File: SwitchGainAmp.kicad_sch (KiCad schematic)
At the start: 22 parts, among them Q3 BSS138, Q4 BSS138, Q5 BSS138, Q6 BSS138, U8 LT1493

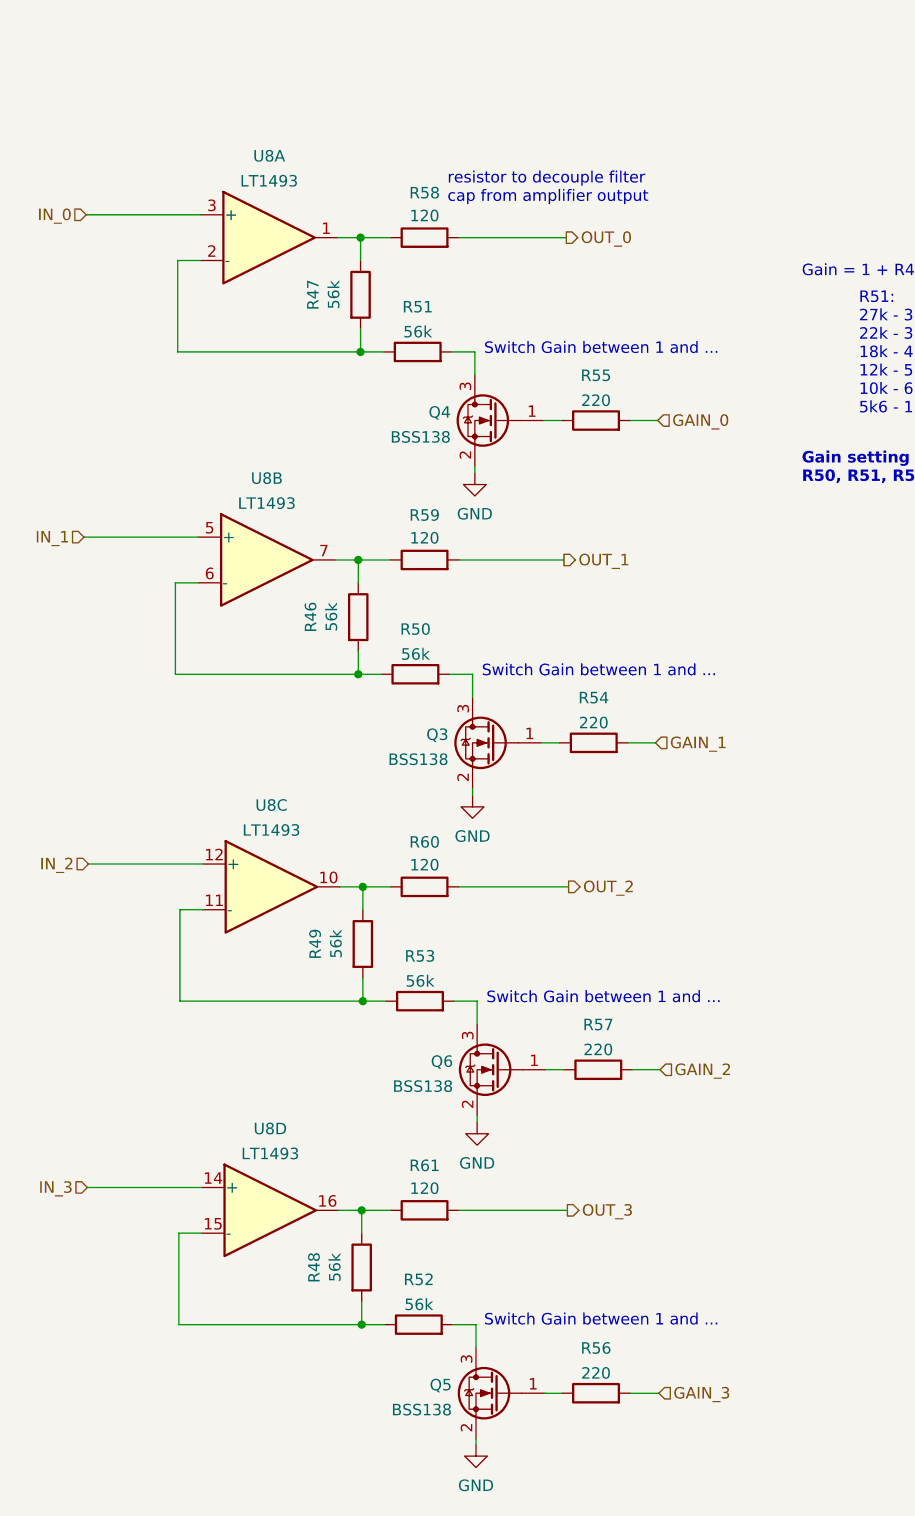
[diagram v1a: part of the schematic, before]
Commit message: aligned to grid
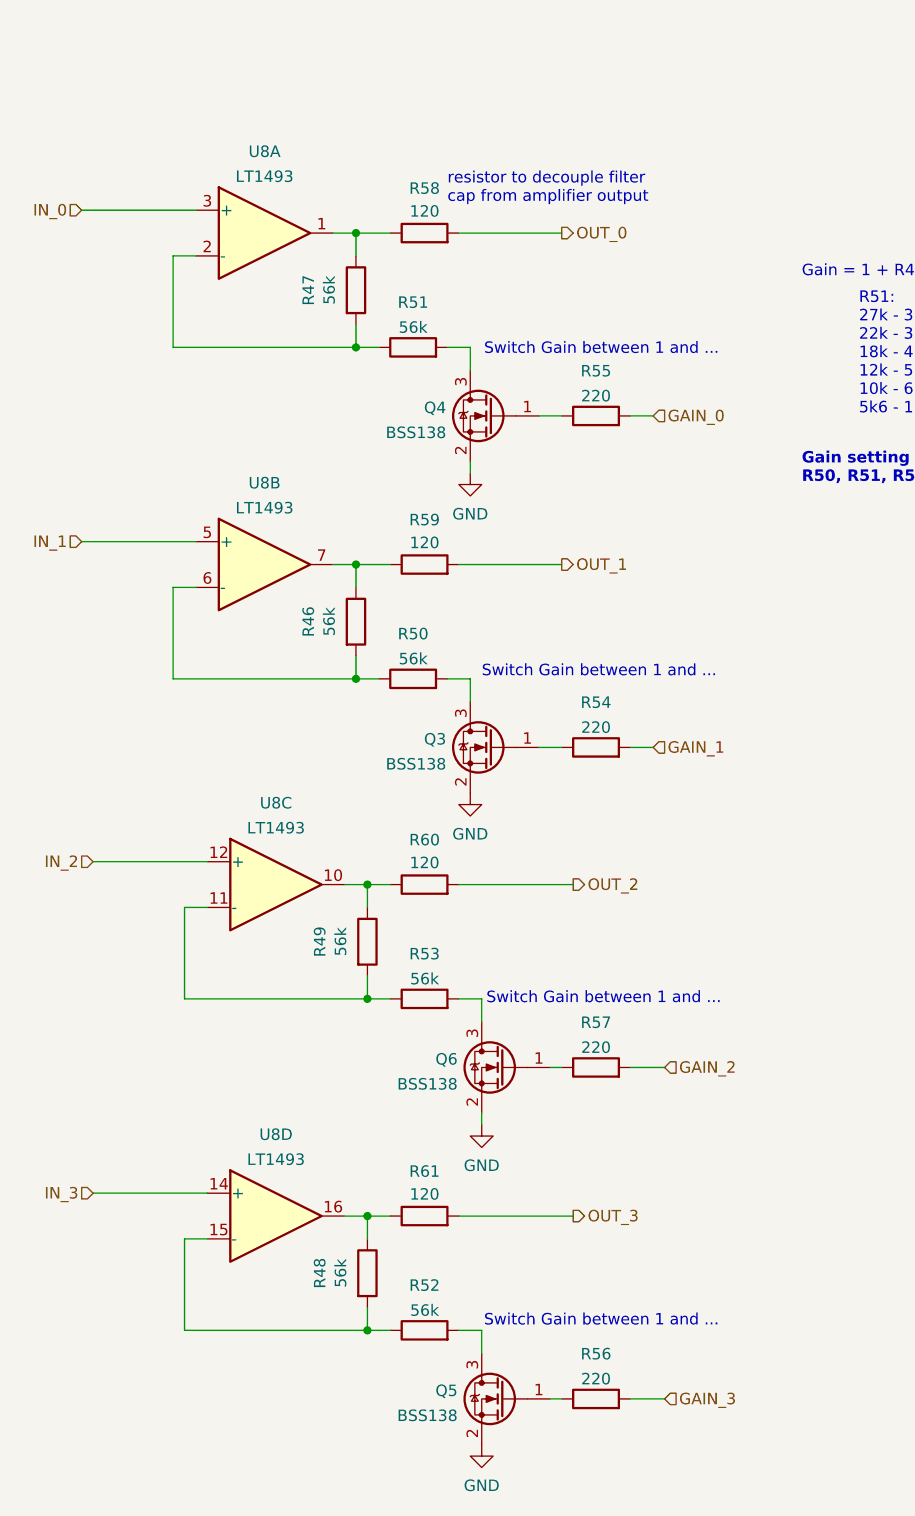
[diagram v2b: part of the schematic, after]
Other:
- moved on the sheet: Q3, Q4, Q5, Q6, R46, R47, R48, R49, R50, R51, R52, R53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

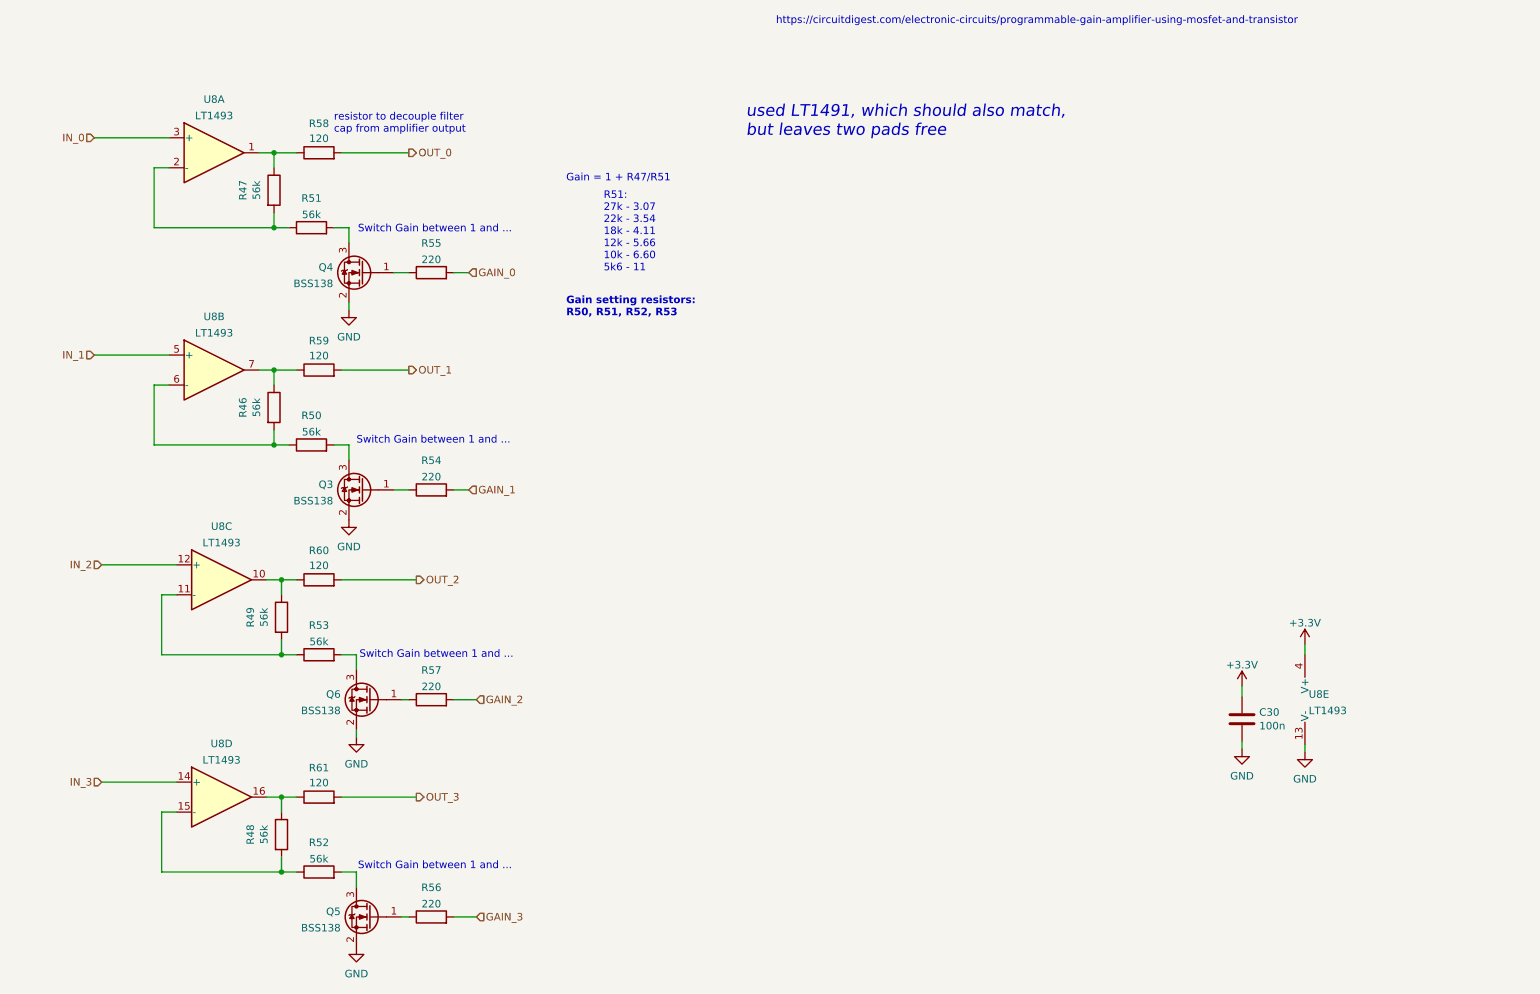
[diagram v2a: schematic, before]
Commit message: updated resistor values to latest findings
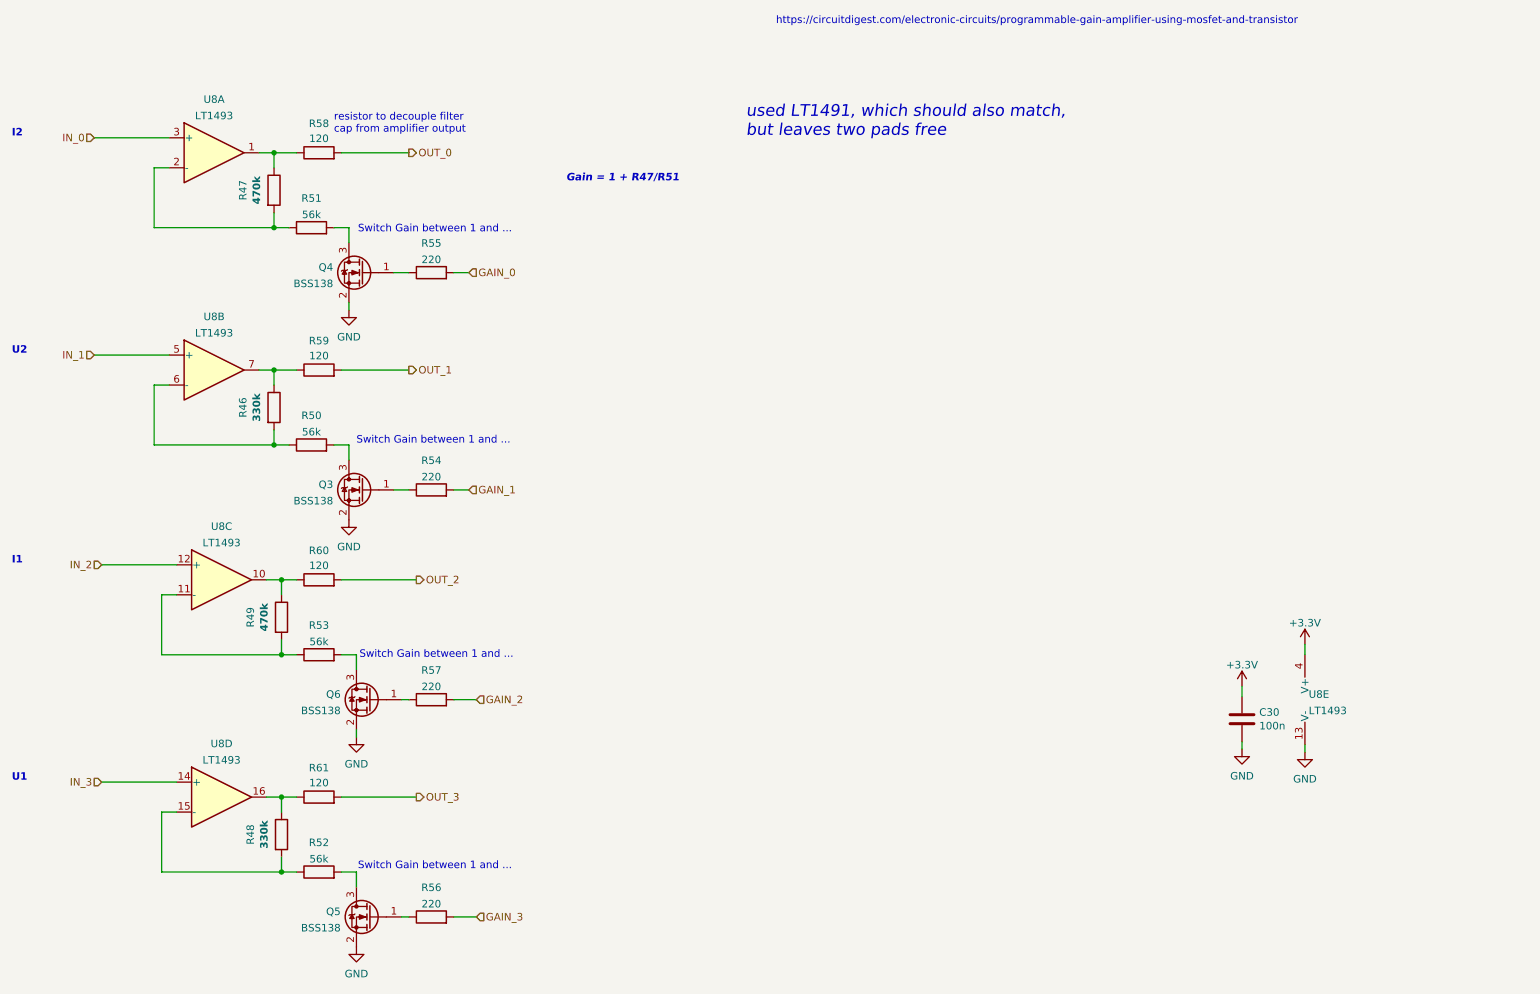
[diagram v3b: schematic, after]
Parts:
- R46, R48: value 56k -> 330k
- R47, R49: value 56k -> 470k
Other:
- note added: "I1"
- note added: "I2"
- note added: "U1"
- note added: "U2"
- note removed: "Gain setting resistors: R50, R51, R52, R53"
- note removed: "R51: 27k - 3.07 22k - 3.54 18k - 4.11 12k - 5.66 10k - 6.60 5k6 - 11"
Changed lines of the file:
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@@
     (stroke (width 0) (type default))
   )
-  (text "Gain setting resistors:\nR50, R51, R52, R53" (at 142.24 67.31 0)
-    (effects (font (size 1.27 1.27) (thickness 0.254) bold) (justify left bottom))
+  (text "U1" (at 48.26 146.05 0)
+    (effects (font (size 1.27 1.27) bold) (justify left bottom))
+  )
+  (text "U2" (at 48.26 73.66 0)
+    (effects (font (size 1.27 1.27) bold) (justify left bottom))
   )
   (text "Switch Gain between 1 and ..." (at 106.68 88.9 0)
@@
     (effects (font (size 1.27 1.27)) (justify left bottom))
   )
+  (text "I2" (at 48.26 36.83 0)
+    (effects (font (size 1.27 1.27) (thickness 0.254) bold) (justify left bottom))
+  )
   (text "Switch Gain between 1 and ..." (at 106.934 53.086 0)
     (effects (font (size 1.27 1.27)) (justify left bottom))
@@
     (effects (font (size 1.27 1.27)) (justify left bottom))
   )
-  (text "R51:\n27k - 3.07\n22k - 3.54\n18k - 4.11\n12k - 5.66\n10k - 6.60\n5k6 - 11"
-    (at 148.59 59.69 0)
-    (effects (font (size 1.27 1.27)) (justify left bottom))
-  )
   (text "Gain = 1 + R47/R51" (at 142.24 44.45 0)
-    (effects (font (size 1.27 1.27)) (justify left bottom))
+    (effects (font (size 1.27 1.27) (thickness 0.254) bold italic) (justify left bottom))
+  )
+  (text "I1" (at 48.26 109.22 0)
+    (effects (font (size 1.27 1.27) bold) (justify left bottom))
   )
   (text "resistor to decouple filter \ncap from amplifier output"
@@
       (effects (font (size 1.27 1.27)))
     )
-    (property "Value" "56k" (at 91.0336 118.11 90)
-      (effects (font (size 1.27 1.27)))
+    (property "Value" "470k" (at 91.0336 118.11 90)
+      (effects (font (size 1.27 1.27) bold))
     )
     (property "Footprint" "Resistor_SMD:R_0603_1608Metric" (at 92.202 118.11 90)
@@
       (effects (font (size 1.27 1.27)))
     )
-    (property "Value" "56k" (at 89.7636 82.55 90)
-      (effects (font (size 1.27 1.27)))
+    (property "Value" "330k" (at 89.7636 82.55 90)
+      (effects (font (size 1.27 1.27) bold))
     )
     (property "Footprint" "Resistor_SMD:R_0603_1608Metric" (at 90.932 82.55 90)
@@
       (effects (font (size 1.27 1.27)))
     )
-    (property "Value" "56k" (at 91.0336 154.94 90)
-      (effects (font (size 1.27 1.27)))
+    (property "Value" "330k" (at 91.0336 154.94 90)
+      (effects (font (size 1.27 1.27) bold))
     )
     (property "Footprint" "Resistor_SMD:R_0603_1608Metric" (at 92.202 154.94 90)
@@
       (effects (font (size 1.27 1.27)))
     )
-    (property "Value" "56k" (at 89.7636 45.72 90)
-      (effects (font (size 1.27 1.27)))
+    (property "Value" "470k" (at 89.7636 45.72 90)
+      (effects (font (size 1.27 1.27) bold))
     )
     (property "Footprint" "Resistor_SMD:R_0603_1608Metric" (at 90.932 45.72 90)

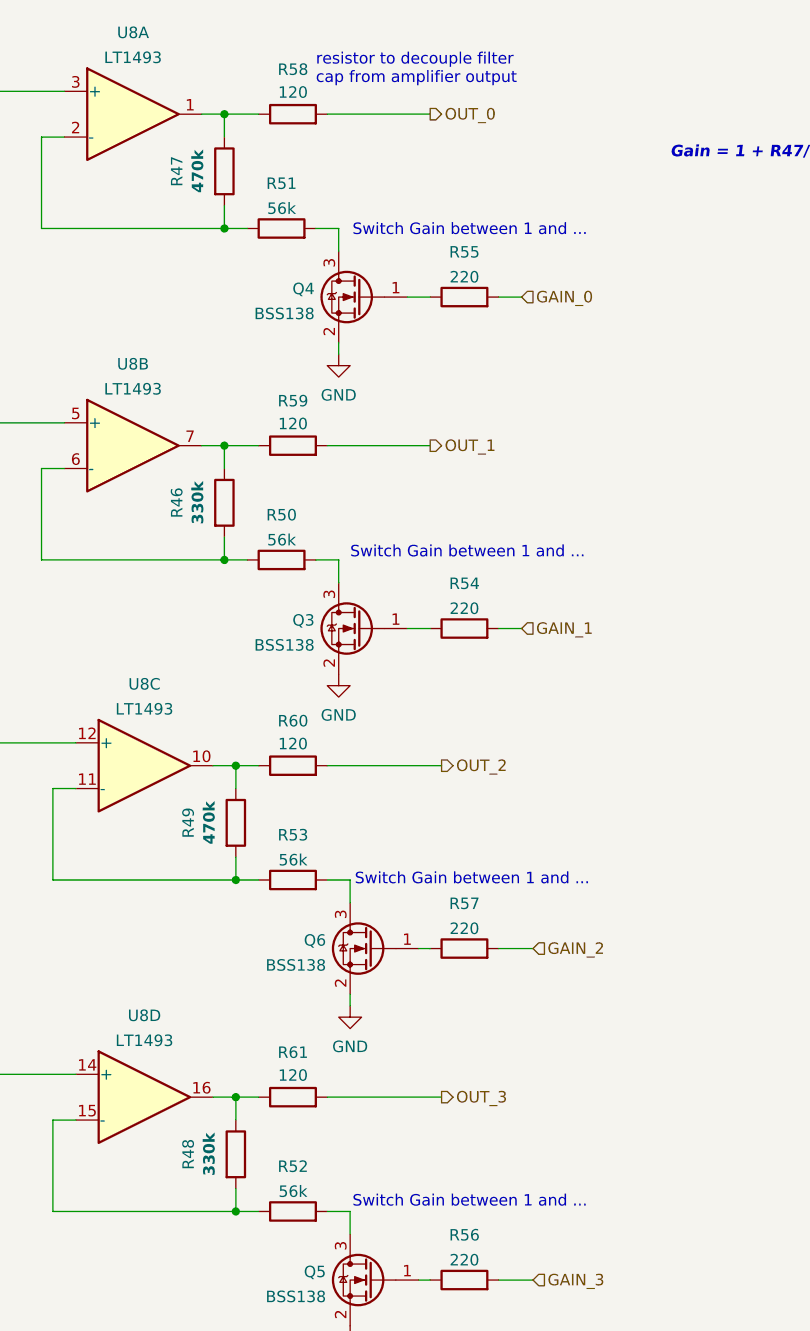
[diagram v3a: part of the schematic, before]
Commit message: added calculated gain to schematic
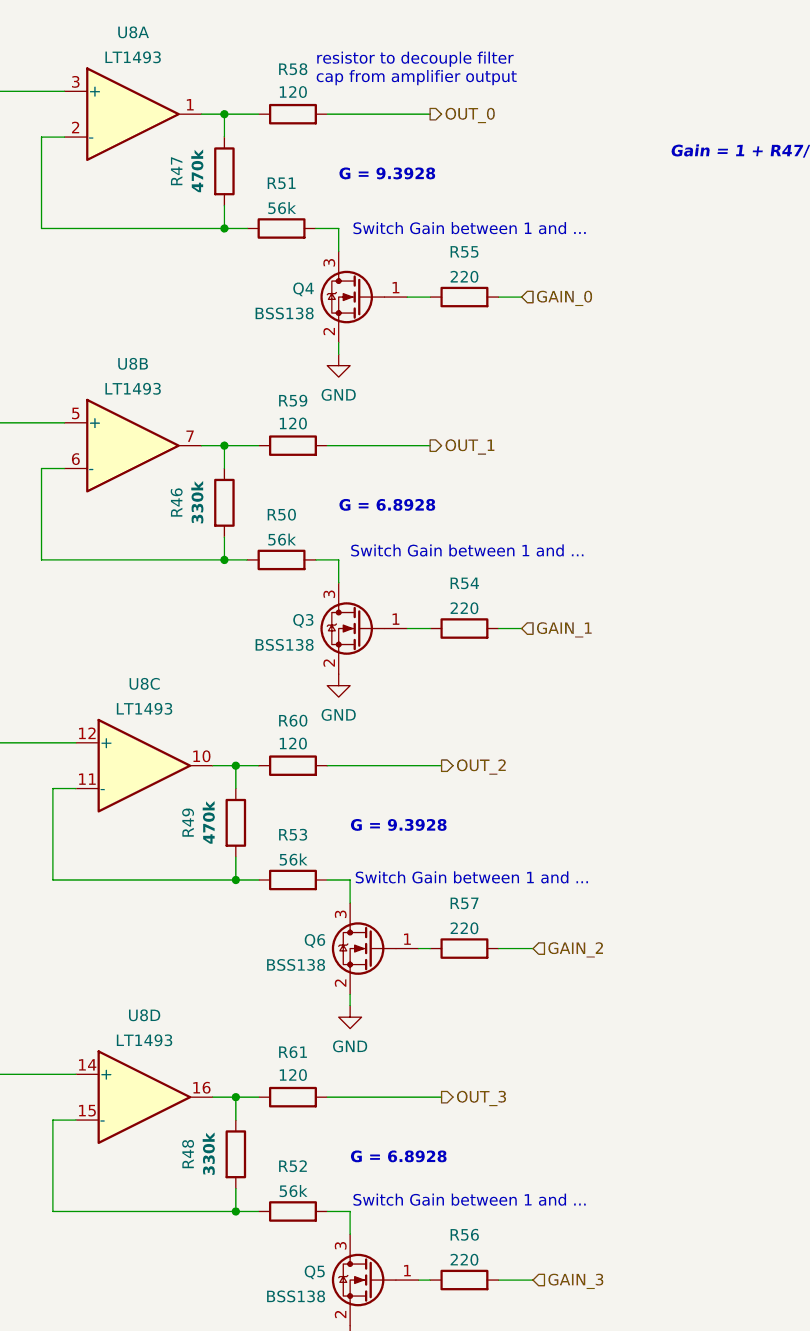
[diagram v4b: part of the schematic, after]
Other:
- note added: "G = 6.8928"
- note added: "G = 9.3928"
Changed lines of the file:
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@@
+    (effects (font (size 1.27 1.27) bold) (justify left bottom))
+  )
+  (text "G = 6.8928" (at 106.68 156.21 0)
     (effects (font (size 1.27 1.27) bold) (justify left bottom))
   )
@@
     (at 177.8 17.78 0)
     (effects (font (size 1.27 1.27)) (justify left bottom))
+  )
+  (text "G = 9.3928" (at 106.68 119.38 0)
+    (effects (font (size 1.27 1.27) bold) (justify left bottom))
   )
   (text "I2" (at 48.26 36.83 0)
@@
     (effects (font (size 2 2) italic) (justify left bottom))
   )
+  (text "G = 9.3928" (at 105.41 46.99 0)
+    (effects (font (size 1.27 1.27) bold) (justify left bottom))
+  )
   (text "Switch Gain between 1 and ..." (at 106.934 161.036 0)
     (effects (font (size 1.27 1.27)) (justify left bottom))
   )
+  (text "G = 6.8928" (at 105.41 83.82 0)
+    (effects (font (size 1.27 1.27) bold) (justify left bottom))
+  )
   (text "Switch Gain between 1 and ..." (at 107.188 125.222 0)
